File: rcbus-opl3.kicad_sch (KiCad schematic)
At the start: 33 parts, among them CON1 3.5mm jack, P1 RC2014 BUS, U1 TL074, U2 YAC512, U3 74HCT688, U4 YMF262, Y1 14.3181MHz

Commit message: add datasheets / farnell links
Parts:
- C1, C10, C2, C7: Farnell_URI (none) -> https://uk.farnell.com/wurth-elektronik/875105240001/cap-10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
- C11, C12, C13, C5, C8: Farnell_URI (none) -> https://uk.farnell.com/multicomp-pro/mc0603b104m250ct/cap-0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
- C3, C4: Farnell_URI (none) -> https://uk.farnell.com/multicomp-pro/mc0603n272j500ct/cap-m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
- C6: Farnell_URI (none) -> https://uk.farnell.com/multicomp-pro/mc0603n680j500ct/cap-6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
- C9: Farnell_URI (none) -> https://uk.farnell.com/kemet/a768eb107m1elas036/cap-100uf-2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
- CON1: Category Connectors, Interconnects -> (none); DK_Datasheet_Link https://www.cui.com/product/resource/digikeypdf/sj1-352xn_s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 -> (none); DK_Detail_Page /product-detail/en/cui-inc/SJ1-3523N/CP1-3523N-ND/738689 -> (none); Digi-Key_PN CP1-3523N-ND -> (none); Family Barrel - Audio Connectors -> (none); Farnell_URI (none) -> https://uk.farnell.com/cliff-electronic-components/fc68131/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; MPN SJ1-3523N -> (none); Manufacturer CUI Inc. -> (none); Status Active -> (none)
- JP1: Farnell_URI (none) -> https://uk.farnell.com/harwin/m20-9980346/connector-header-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
- P1: Farnell_URI (none) -> https://uk.farnell.com/wurth-elektronik/61304011021/header-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
- R1: Farnell_URI (none) -> https://uk.farnell.com/multicomp-pro/mcwr06x33r0ftl/res-33r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
- R10, R11, R2, R5, R6, R7, R8, R9: Farnell_URI (none) -> https://uk.farnell.com/multicomp-pro/mcwr06x1002ftl/res-10k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
- R3, R4: Farnell_URI (none) -> https://uk.farnell.com/multicomp-pro/mcwr06x1000ftl/res-100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
- U1: Farnell_URI (none) -> https://uk.farnell.com/stmicroelectronics/tl074cdt/opamp-3m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
- U3: Farnell_URI (none) -> https://uk.farnell.com/texas-instruments/cd74hct688m96/comp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
- Y1: Farnell_URI (none) -> https://uk.farnell.com/multicomp-pro/mcsjk-6nc1-14-31818-25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
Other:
- moved on the sheet: C2, C7, CON1, R2, R3, R4, R5

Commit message: update the parts for the large caps
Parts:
- C1, C10, C2, C7: Farnell_URI https://uk.farnell.com/wurth-elektronik/875105240001/cap-10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 -> https://uk.farnell.com/kemet/edk106m035a9baa/cap-10uf-35v-a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
- C9: Farnell_URI https://uk.farnell.com/kemet/a768eb107m1elas036/cap-100uf-2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 -> https://uk.farnell.com/kemet/edk107m035a9haa/cap-100-f-35v-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
- JP1: value BASE ADDRESS -> 2x06 pin header
- P1: value RC2014 BUS -> 1x39 pin header
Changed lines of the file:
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@@
 			)
 		)
-		(property "Value" "RC2014 BUS"
+		(property "Value" "1x39 pin header"
 			(at 24.13 69.85 90)
 			(effects
@@
 			)
 		)
-		(property "Description" "Generic connector, single row, 01x39, script generated (kicad-library-utils/schlib/autogen/connector/)"
+		(property "Description" "Generic connector, single row, 01x39"
 			(at 26.67 69.85 0)
 			(effects
@@
 			)
 		)
-		(property "Value" "BASE ADDRESS"
+		(property "Value" "2x06 pin header"
 			(at 80.01 67.31 90)
 			(effects
@@
 			)
 		)
-		(property "Description" "Generic connector, double row, 02x06, odd/even pin numbering scheme (row 1 odd numbers, row 2 even numbers), script generated (kicad-library-utils/schlib/autogen/connector/)"
+		(property "Description" "Generic connector, double row, 02x06"
 			(at 81.28 67.31 0)
 			(effects
@@
 			)
 		)
-		(property "Datasheet" "https://search.kemet.com/component-documentation/download/specsheet/A768EB107M1ELAS036"
+		(property "Datasheet" "https://content.kemet.com/datasheets/KEM_A4001_EDK.pdf"
 			(at 50.8 73.66 0)
 			(effects
@@
 			)
 		)
-		(property "Farnell_URI" "https://uk.farnell.com/kemet/a768eb107m1elas036/cap-100uf-25v-alu-elec-smd-polymer/dp/4071180"
+		(property "Farnell_URI" "https://uk.farnell.com/kemet/edk107m035a9haa/cap-100-f-35v-radial-smd-reel/dp/2068675"
 			(at 50.8 73.66 0)
 			(effects
@@
 			)
 		)
-		(property "Datasheet" "https://www.we-online.com/components/products/datasheet/875105240001.pdf"
+		(property "Datasheet" "https://content.kemet.com/datasheets/KEM_A4001_EDK.pdf"
 			(at 233.68 33.02 0)
 			(effects
@@
 			)
 		)
-		(property "Farnell_URI" "https://uk.farnell.com/wurth-elektronik/875105240001/cap-10-f-10v-20/dp/2466639"
+		(property "Farnell_URI" "https://uk.farnell.com/kemet/edk106m035a9baa/cap-10uf-35v-alu-elec-smd/dp/4144058"
 			(at 233.68 33.02 0)
 			(effects
@@
 			)
 		)
-		(property "Datasheet" "https://www.we-online.com/components/products/datasheet/875105240001.pdf"
+		(property "Datasheet" "https://content.kemet.com/datasheets/KEM_A4001_EDK.pdf"
 			(at 199.39 134.62 0)
 			(effects
@@
 			)
 		)
-		(property "Farnell_URI" "https://uk.farnell.com/wurth-elektronik/875105240001/cap-10-f-10v-20/dp/2466639"
+		(property "Farnell_URI" "https://uk.farnell.com/kemet/edk106m035a9baa/cap-10uf-35v-alu-elec-smd/dp/4144058"
 			(at 199.39 134.62 90)
 			(effects
@@
 			)
 		)
-		(property "Description" "Resistor, small symbol"
+		(property "Description" "Resistor"
 			(at 97.79 78.74 0)
 			(effects
@@
 			)
 		)
-		(property "Description" "Resistor, small symbol"
+		(property "Description" "Resistor"
 			(at 113.03 78.74 0)
 			(effects
@@
 			)
 		)
-		(property "Description" "Resistor, small symbol"
+		(property "Description" "Resistor"
 			(at 87.63 78.74 0)
 			(effects
@@
 			)
 		)
-		(property "Description" "Resistor, small symbol"
+		(property "Description" "Resistor"
 			(at 107.95 78.74 0)
 			(effects
@@
 			)
 		)
-		(property "Datasheet" "https://www.we-online.com/components/products/datasheet/875105240001.pdf"
+		(property "Datasheet" "https://content.kemet.com/datasheets/KEM_A4001_EDK.pdf"
 			(at 58.42 73.66 0)
 			(effects
@@
 			)
 		)
-		(property "Farnell_URI" "https://uk.farnell.com/wurth-elektronik/875105240001/cap-10-f-10v-20/dp/2466639"
+		(property "Farnell_URI" "https://uk.farnell.com/kemet/edk106m035a9baa/cap-10uf-35v-alu-elec-smd/dp/4144058"
 			(at 58.42 73.66 0)
 			(effects
@@
 			)
 		)
-		(property "Description" "Resistor, small symbol"
+		(property "Description" "Resistor"
 			(at 92.71 78.74 0)
 			(effects
@@
 			)
 		)
-		(property "Description" "3.3V HCMOS SMD Crystal Clock Oscillator, Abracon"
+		(property "Description" "5v oscillator"
 			(at 82.55 167.64 0)
 			(effects
@@
 			)
 		)
-		(property "Description" ""
+		(property "Description" "D/A Converter"
 			(at 195.58 78.486 0)
 			(effects
@@
 			)
 		)
-		(property "Description" ""
+		(property "Description" "OPL3 FM Synthesis IC"
 			(at 119.38 162.306 0)
 			(effects
@@
 			)
 		)
-		(property "Datasheet" "https://www.we-online.com/components/products/datasheet/875105240001.pdf"
+		(property "Datasheet" "https://content.kemet.com/datasheets/KEM_A4001_EDK.pdf"
 			(at 199.39 149.86 0)
 			(effects
@@
 			)
 		)
-		(property "Farnell_URI" "https://uk.farnell.com/wurth-elektronik/875105240001/cap-10-f-10v-20/dp/2466639"
+		(property "Farnell_URI" "https://uk.farnell.com/kemet/edk106m035a9baa/cap-10uf-35v-alu-elec-smd/dp/4144058"
 			(at 199.39 149.86 90)
 			(effects
@@
 			)
 		)
-		(property "Description" "Resistor, small symbol"
+		(property "Description" "Resistor"
 			(at 102.87 78.74 0)
 			(effects

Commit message: add mpn field
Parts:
- C1, C10, C2, C7: MPN (none) -> EDK106M035A9BAA
- C11, C12, C13, C5, C8: MPN (none) -> MC0603B104M250CT
- C3, C4: MPN (none) -> MC0603N272J500CT
- C6: MPN (none) -> MC0603N680J500CT
- C9: MPN (none) -> EDK107M035A9HAA
- CON1: MPN (none) -> FC68131
- JP1: MPN (none) -> M20-9980346
- P1: MPN (none) -> 61304011021
- R1: MPN (none) -> MCWR06X33R0FTL
- R10, R11, R2, R5, R6, R7, R8, R9: MPN (none) -> MCWR06X1002FTL
- R3, R4: MPN (none) -> MCWR06X1000FTL
- U1: MPN (none) -> TL074CDT
- U3: MPN (none) -> CD74HCT688M96
- Y1: MPN (none) -> MCSJK-6NC1-14.31818-25-B

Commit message: some r2 changes
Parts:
- U2: footprint Package_SO:SOP-16_4.55x10.3mm_P1.27mm -> Package_SO:SOIC-16W_5.3x10.2mm_P1.27mm
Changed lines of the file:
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@@
 			)
 		)
-		(property "Footprint" "Package_SO:SOP-16_4.55x10.3mm_P1.27mm"
+		(property "Footprint" "Package_SO:SOIC-16W_5.3x10.2mm_P1.27mm"
 			(at 195.326 97.282 0)
 			(effects

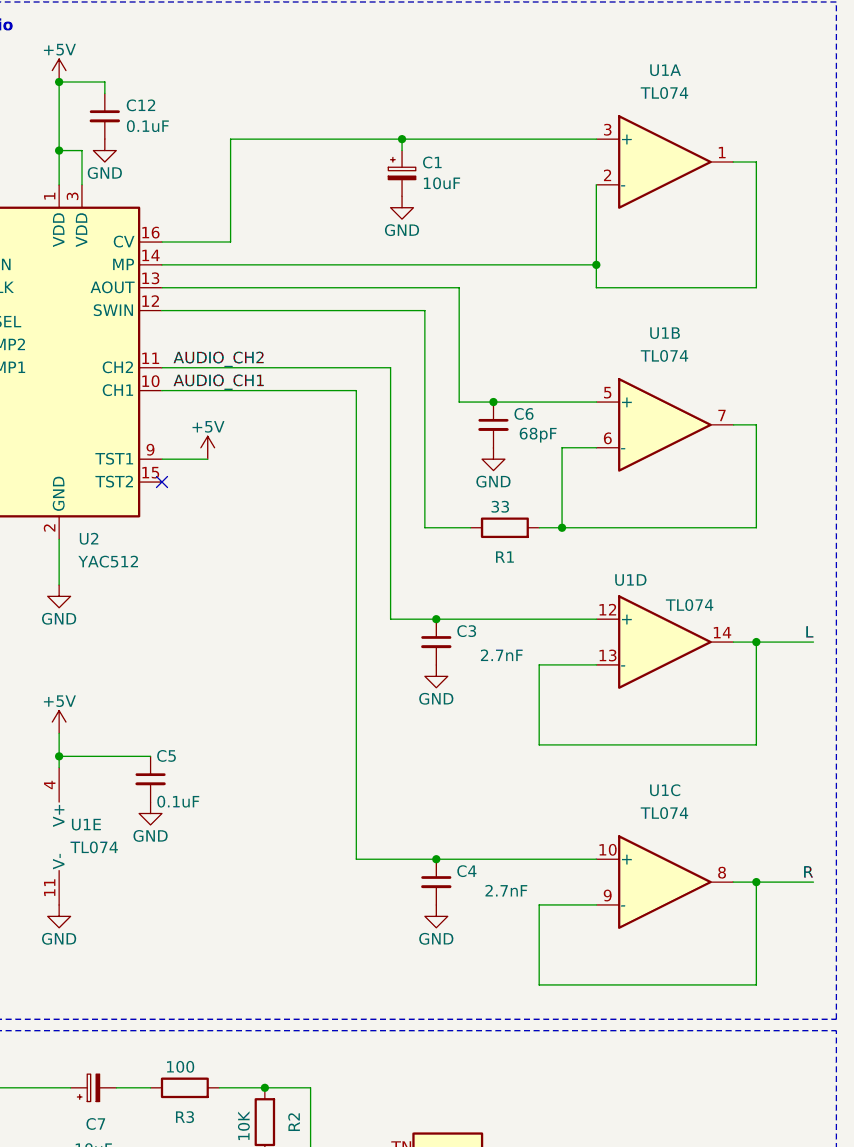
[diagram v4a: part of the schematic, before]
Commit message: wip: change 10uf electrolytics to 4mm diameter, and use custom footprint for ymf262
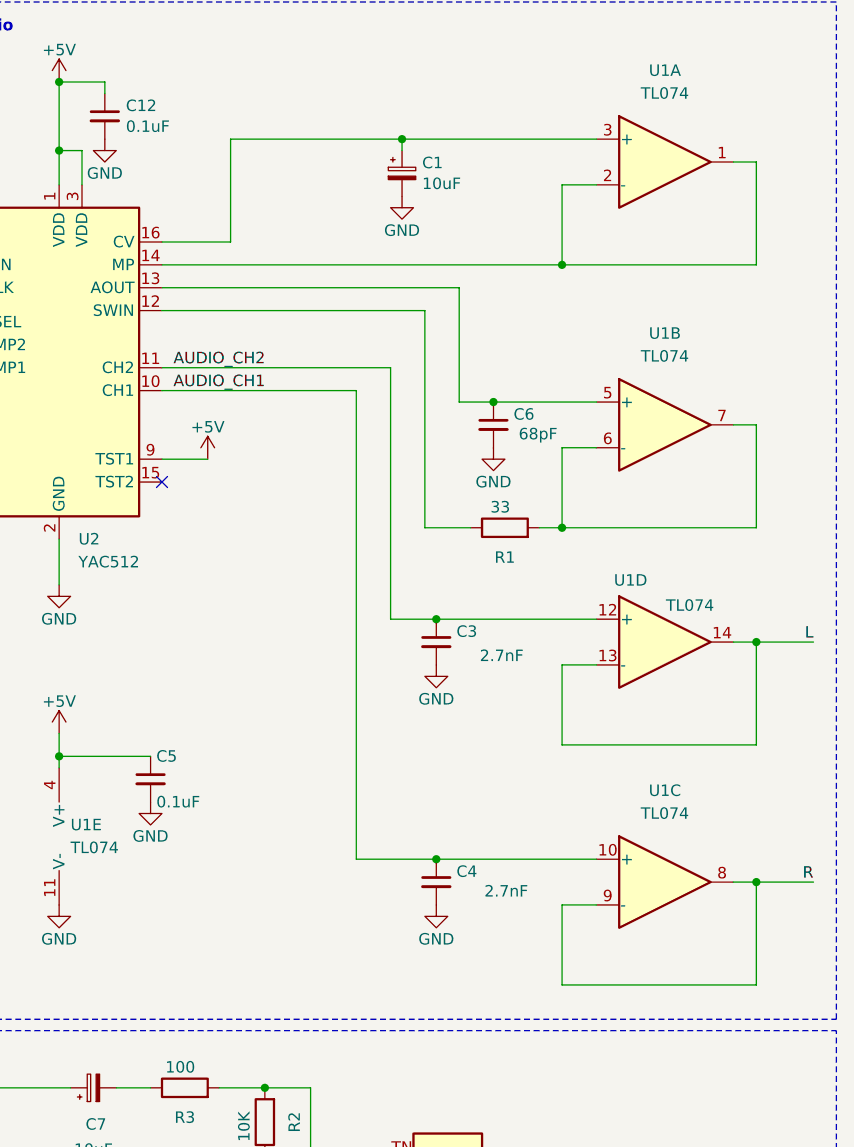
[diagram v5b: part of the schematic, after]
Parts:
- C1, C10, C2, C7: footprint Capacitor_SMD:CP_Elec_6.3x5.8 -> Capacitor_SMD:CP_Elec_4x5.4
- U4: footprint Package_SO:SOP-24_7.5x15.4mm_P1.27mm -> electrified:SOP-24_wider
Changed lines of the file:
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@@
 	)
 	(junction
-		(at 255.27 43.18)
-		(diameter 0)
-		(color 0 0 0 0)
-	)
-	(junction
 		(at 87.63 59.69)
 		(diameter 0)
@@
 	)
 	(junction
+		(at 251.46 43.18)
+		(diameter 0)
+		(color 0 0 0 0)
+	)
+	(junction
 		(at 232.41 149.86)
 		(diameter 0)
@@
 		)
 	)
-	(wire
+	(polyline
 		(pts
-			(xy 255.27 43.18) (xy 255.27 45.72)
+			(xy 62.23 99.06) (xy 62.23 186.69)
 		)
 		(stroke
 			(width 0)
-			(type default)
+			(type dash)
 		)
 	)
-	(polyline
+	(wire
 		(pts
-			(xy 62.23 99.06) (xy 62.23 186.69)
+			(xy 101.6 161.29) (xy 107.95 161.29)
 		)
 		(stroke
 			(width 0)
-			(type dash)
+			(type default)
 		)
 	)
 	(wire
 		(pts
-			(xy 101.6 161.29) (xy 107.95 161.29)
+			(xy 251.46 34.29) (xy 255.27 34.29)
 		)
 		(stroke
@@
 	(wire
 		(pts
-			(xy 248.92 123.19) (xy 248.92 114.3)
+			(xy 251.46 123.19) (xy 251.46 114.3)
 		)
 		(stroke
@@
 	(wire
 		(pts
-			(xy 248.92 96.52) (xy 273.05 96.52)
+			(xy 251.46 96.52) (xy 273.05 96.52)
 		)
 		(stroke
@@
 	(wire
 		(pts
-			(xy 207.01 43.18) (xy 255.27 43.18)
+			(xy 207.01 43.18) (xy 251.46 43.18)
 		)
 		(stroke
@@
 	(wire
 		(pts
-			(xy 248.92 123.19) (xy 273.05 123.19)
+			(xy 251.46 123.19) (xy 273.05 123.19)
 		)
 		(stroke
@@
 	(wire
 		(pts
-			(xy 273.05 31.75) (xy 273.05 45.72)
+			(xy 273.05 31.75) (xy 273.05 43.18)
 		)
 		(stroke
@@
 	(wire
 		(pts
-			(xy 248.92 87.63) (xy 255.27 87.63)
+			(xy 251.46 87.63) (xy 255.27 87.63)
 		)
 		(stroke
@@
 	(wire
 		(pts
-			(xy 255.27 34.29) (xy 255.27 43.18)
+			(xy 251.46 34.29) (xy 251.46 43.18)
 		)
 		(stroke
@@
 	(wire
 		(pts
-			(xy 273.05 45.72) (xy 255.27 45.72)
+			(xy 273.05 43.18) (xy 251.46 43.18)
 		)
 		(stroke
@@
 	(wire
 		(pts
-			(xy 248.92 96.52) (xy 248.92 87.63)
+			(xy 251.46 96.52) (xy 251.46 87.63)
 		)
 		(stroke
@@
 	(wire
 		(pts
-			(xy 248.92 114.3) (xy 255.27 114.3)
+			(xy 251.46 114.3) (xy 255.27 114.3)
 		)
 		(stroke
@@
 			)
 		)
-		(property "Footprint" "Capacitor_SMD:CP_Elec_6.3x5.8"
+		(property "Footprint" "Capacitor_SMD:CP_Elec_4x5.4"
 			(at 233.68 33.02 0)
 			(effects
@@
 			)
 		)
-		(property "Footprint" "Capacitor_SMD:CP_Elec_6.3x5.8"
+		(property "Footprint" "Capacitor_SMD:CP_Elec_4x5.4"
 			(at 199.39 134.62 0)
 			(effects
@@
 			)
 		)
-		(property "Footprint" "Capacitor_SMD:CP_Elec_6.3x5.8"
+		(property "Footprint" "Capacitor_SMD:CP_Elec_4x5.4"
 			(at 58.42 73.66 0)
 			(effects
@@
 			)
 		)
-		(property "Footprint" "Package_SO:SOP-24_7.5x15.4mm_P1.27mm"
+		(property "Footprint" "electrified:SOP-24_wider"
 			(at 119.126 181.102 0)
 			(effects
@@
 			)
 		)
-		(property "Footprint" "Capacitor_SMD:CP_Elec_6.3x5.8"
+		(property "Footprint" "Capacitor_SMD:CP_Elec_4x5.4"
 			(at 199.39 149.86 0)
 			(effects

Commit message: update symbols/footprints to kicad 9.0.7, improve ymf footprint
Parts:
- U2: footprint Package_SO:SOIC-16W_5.3x10.2mm_P1.27mm -> Package_SO:SOP-16_4.55x10.3mm_P1.27mm
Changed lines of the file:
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@@
 			)
 		)
-		(property "Datasheet" "https://www.we-online.com/components/products/datasheet/61304011021.pdf"
+		(property "Datasheet" "~"
 			(at 26.67 69.85 0)
 			(effects
@@
 			)
 		)
-		(property "Description" "Generic connector, single row, 01x39"
+		(property "Description" "Generic connector, single row, 01x39, script generated (kicad-library-utils/schlib/autogen/connector/)"
 			(at 26.67 69.85 0)
 			(effects
@@
 			)
 		)
-		(property "Datasheet" "https://4donline.ihs.com/images/VipMasterIC/IC/SCMP/SCMP-S-A0009426256/SCMP-S-A0009474646-1.pdf?hkey=6D3A4C79FDBF58556ACFDE234799DDF0"
+		(property "Datasheet" "~"
 			(at 132.08 25.4 0)
 			(effects
@@
 			)
 		)
-		(property "Datasheet" "https://4donline.ihs.com/images/VipMasterIC/IC/SCMP/SCMP-S-A0009426256/SCMP-S-A0009474646-1.pdf?hkey=6D3A4C79FDBF58556ACFDE234799DDF0"
+		(property "Datasheet" "~"
 			(at 113.03 110.49 0)
 			(effects
@@
 			)
 		)
-		(property "Datasheet" "https://4donline.ihs.com/images/VipMasterIC/IC/HRWN/HRWN-S-A0001370718/HRWN-S-A0009370459-1.pdf?hkey=6D3A4C79FDBF58556ACFDE234799DDF0"
+		(property "Datasheet" "~"
 			(at 81.28 67.31 0)
 			(effects
@@
 			)
 		)
-		(property "Description" "Generic connector, double row, 02x06"
+		(property "Description" "Generic connector, double row, 02x06, odd/even pin numbering scheme (row 1 odd numbers, row 2 even numbers), script generated (kicad-library-utils/schlib/autogen/connector/)"
 			(at 81.28 67.31 0)
 			(effects
@@
 			)
 		)
-		(property "Datasheet" "https://4donline.ihs.com/images/VipMasterIC/IC/SCMP/SCMP-S-A0009426256/SCMP-S-A0009474646-1.pdf?hkey=6D3A4C79FDBF58556ACFDE234799DDF0"
+		(property "Datasheet" "~"
 			(at 205.74 100.33 0)
 			(effects
@@
 			)
 		)
-		(property "Datasheet" "https://content.kemet.com/datasheets/KEM_A4001_EDK.pdf"
+		(property "Datasheet" "~"
 			(at 50.8 73.66 0)
 			(effects
@@
 			)
 		)
-		(property "Datasheet" "https://www.farnell.com/datasheets/2028381.pdf"
+		(property "Datasheet" "~"
 			(at 237.49 149.86 0)
 			(effects
@@
 			)
 		)
-		(property "Datasheet" "https://4donline.ihs.com/images/VipMasterIC/IC/SCMP/SCMP-S-A0009426256/SCMP-S-A0009474646-1.pdf?hkey=6D3A4C79FDBF58556ACFDE234799DDF0"
+		(property "Datasheet" "~"
 			(at 200.66 26.67 0)
 			(effects
@@
 			)
 		)
-		(property "Datasheet" "https://content.kemet.com/datasheets/KEM_A4001_EDK.pdf"
+		(property "Datasheet" "~"
 			(at 233.68 33.02 0)
 			(effects
@@
 			)
 		)
-		(property "Datasheet" "https://content.kemet.com/datasheets/KEM_A4001_EDK.pdf"
+		(property "Datasheet" "~"
 			(at 199.39 134.62 0)
 			(effects
@@
 			)
 		)
-		(property "Datasheet" "https://4donline.ihs.com/images/VipMasterIC/IC/SCMP/SCMP-S-A0009547702/SCMP-S-A0009547702-1.pdf?hkey=6D3A4C79FDBF58556ACFDE234799DDF0"
+		(property "Datasheet" "~"
 			(at 218.44 138.43 0)
 			(effects
@@
 			)
 		)
-		(property "Datasheet" "https://www.farnell.com/datasheets/4417444.pdf"
+		(property "Datasheet" "~"
 			(at 237.49 111.76 0)
 			(effects
@@
 			)
 		)
-		(property "Datasheet" "https://4donline.ihs.com/images/VipMasterIC/IC/SCMP/SCMP-S-A0009547702/SCMP-S-A0009547702-1.pdf?hkey=6D3A4C79FDBF58556ACFDE234799DDF0"
+		(property "Datasheet" "~"
 			(at 97.79 78.74 0)
 			(effects
@@
 			)
 		)
-		(property "Description" "Resistor"
+		(property "Description" "Resistor, small symbol"
 			(at 97.79 78.74 0)
 			(effects
@@
 			)
 		)
-		(property "Datasheet" "https://4donline.ihs.com/images/VipMasterIC/IC/SCMP/SCMP-S-A0009547702/SCMP-S-A0009547702-1.pdf?hkey=6D3A4C79FDBF58556ACFDE234799DDF0"
+		(property "Datasheet" "~"
 			(at 113.03 78.74 0)
 			(effects
@@
 			)
 		)
-		(property "Description" "Resistor"
+		(property "Description" "Resistor, small symbol"
 			(at 113.03 78.74 0)
 			(effects
@@
 			)
 		)
-		(property "Datasheet" "https://4donline.ihs.com/images/VipMasterIC/IC/SCMP/SCMP-S-A0009547702/SCMP-S-A0009547702-1.pdf?hkey=6D3A4C79FDBF58556ACFDE234799DDF0"
+		(property "Datasheet" "~"
 			(at 87.63 78.74 0)
 			(effects
@@
 			)
 		)
-		(property "Description" "Resistor"
+		(property "Description" "Resistor, small symbol"
 			(at 87.63 78.74 0)
 			(effects
@@
 			)
 		)
-		(property "Datasheet" "https://4donline.ihs.com/images/VipMasterIC/IC/SCMP/SCMP-S-A0009547702/SCMP-S-A0009547702-1.pdf?hkey=6D3A4C79FDBF58556ACFDE234799DDF0"
+		(property "Datasheet" "~"
 			(at 107.95 78.74 0)
 			(effects
@@
 			)
 		)
-		(property "Description" "Resistor"
+		(property "Description" "Resistor, small symbol"
 			(at 107.95 78.74 0)
 			(effects
@@
 			)
 		)
-		(property "Datasheet" "https://content.kemet.com/datasheets/KEM_A4001_EDK.pdf"
+		(property "Datasheet" "~"
 			(at 58.42 73.66 0)
 			(effects
@@
 			)
 		)
-		(property "Datasheet" "https://4donline.ihs.com/images/VipMasterIC/IC/SCMP/SCMP-S-A0009547702/SCMP-S-A0009547702-1.pdf?hkey=6D3A4C79FDBF58556ACFDE234799DDF0"
+		(property "Datasheet" "~"
 			(at 92.71 78.74 0)
 			(effects
@@
 			)
 		)
-		(property "Description" "Resistor"
+		(property "Description" "Resistor, small symbol"
 			(at 92.71 78.74 0)
 			(effects
@@
 			)
 		)
-		(property "Datasheet" "https://4donline.ihs.com/images/VipMasterIC/IC/SCMP/SCMP-S-A0009547702/SCMP-S-A0009547702-1.pdf?hkey=6D3A4C79FDBF58556ACFDE234799DDF0"
+		(property "Datasheet" "~"
 			(at 218.44 153.67 0)
 			(effects
@@
 			)
 		)
-		(property "Datasheet" "https://4donline.ihs.com/images/VipMasterIC/IC/SCMP/SCMP-S-A0010069830/SCMP-S-A0010069830-1.pdf?hkey=6D3A4C79FDBF58556ACFDE234799DDF0"
+		(property "Datasheet" "http://www.abracon.com/Oscillators/ASV.pdf"
 			(at 80.01 167.64 0)
 			(effects
@@
 			)
 		)
-		(property "Description" "5v oscillator"
+		(property "Description" "3.3V HCMOS SMD Crystal Clock Oscillator, Abracon"
 			(at 82.55 167.64 0)
 			(effects
@@
 			)
 		)
-		(property "Footprint" "Package_SO:SOIC-16W_5.3x10.2mm_P1.27mm"
+		(property "Footprint" "Package_SO:SOP-16_4.55x10.3mm_P1.27mm"
 			(at 195.326 97.282 0)
 			(effects
@@
 			)
 		)
-		(property "Datasheet" "https://4donline.ihs.com/images/VipMasterIC/IC/SCMP/SCMP-S-A0009426256/SCMP-S-A0009474646-1.pdf?hkey=6D3A4C79FDBF58556ACFDE234799DDF0"
+		(property "Datasheet" "~"
 			(at 87.63 153.67 0)
 			(effects
@@
 			)
 		)
-		(property "Datasheet" "https://4donline.ihs.com/images/VipMasterIC/IC/SCMP/SCMP-S-A0009547702/SCMP-S-A0009547702-1.pdf?hkey=6D3A4C79FDBF58556ACFDE234799DDF0"
+		(property "Datasheet" "~"
 			(at 245.11 72.39 0)
 			(effects
@@
 			)
 		)
-		(property "Datasheet" "https://4donline.ihs.com/images/VipMasterIC/IC/SCMP/SCMP-S-A0009547702/SCMP-S-A0009547702-1.pdf?hkey=6D3A4C79FDBF58556ACFDE234799DDF0"
+		(property "Datasheet" "~"
 			(at 209.55 134.62 0)
 			(effects
@@
 			)
 		)
-		(property "Datasheet" "https://4donline.ihs.com/images/VipMasterIC/IC/SCMP/SCMP-S-A0009547702/SCMP-S-A0009547702-1.pdf?hkey=6D3A4C79FDBF58556ACFDE234799DDF0"
+		(property "Datasheet" "~"
 			(at 209.55 149.86 0)
 			(effects
@@
 			)
 		)
-		(property "Datasheet" "https://www.farnell.com/datasheets/4417444.pdf"
+		(property "Datasheet" "~"
 			(at 243.84 60.96 0)
 			(effects
@@
 			)
 		)
-		(property "Datasheet" "https://www.farnell.com/datasheets/4417444.pdf"
+		(property "Datasheet" "~"
 			(at 237.49 85.09 0)
 			(effects
@@
 			)
 		)
-		(property "Datasheet" "https://content.kemet.com/datasheets/KEM_A4001_EDK.pdf"
+		(property "Datasheet" "~"
 			(at 199.39 149.86 0)
 			(effects
@@
 			)
 		)
-		(property "Datasheet" "https://4donline.ihs.com/images/VipMasterIC/IC/SCMP/SCMP-S-A0009547702/SCMP-S-A0009547702-1.pdf?hkey=6D3A4C79FDBF58556ACFDE234799DDF0"
+		(property "Datasheet" "~"
 			(at 102.87 78.74 0)
 			(effects
@@
 			)
 		)
-		(property "Description" "Resistor"
+		(property "Description" "Resistor, small symbol"
 			(at 102.87 78.74 0)
 			(effects
